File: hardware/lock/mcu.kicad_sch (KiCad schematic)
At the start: 7 parts, among them J2 DIGITAL IF (auth), J4 UPDI PROG, U1 ATtiny1616

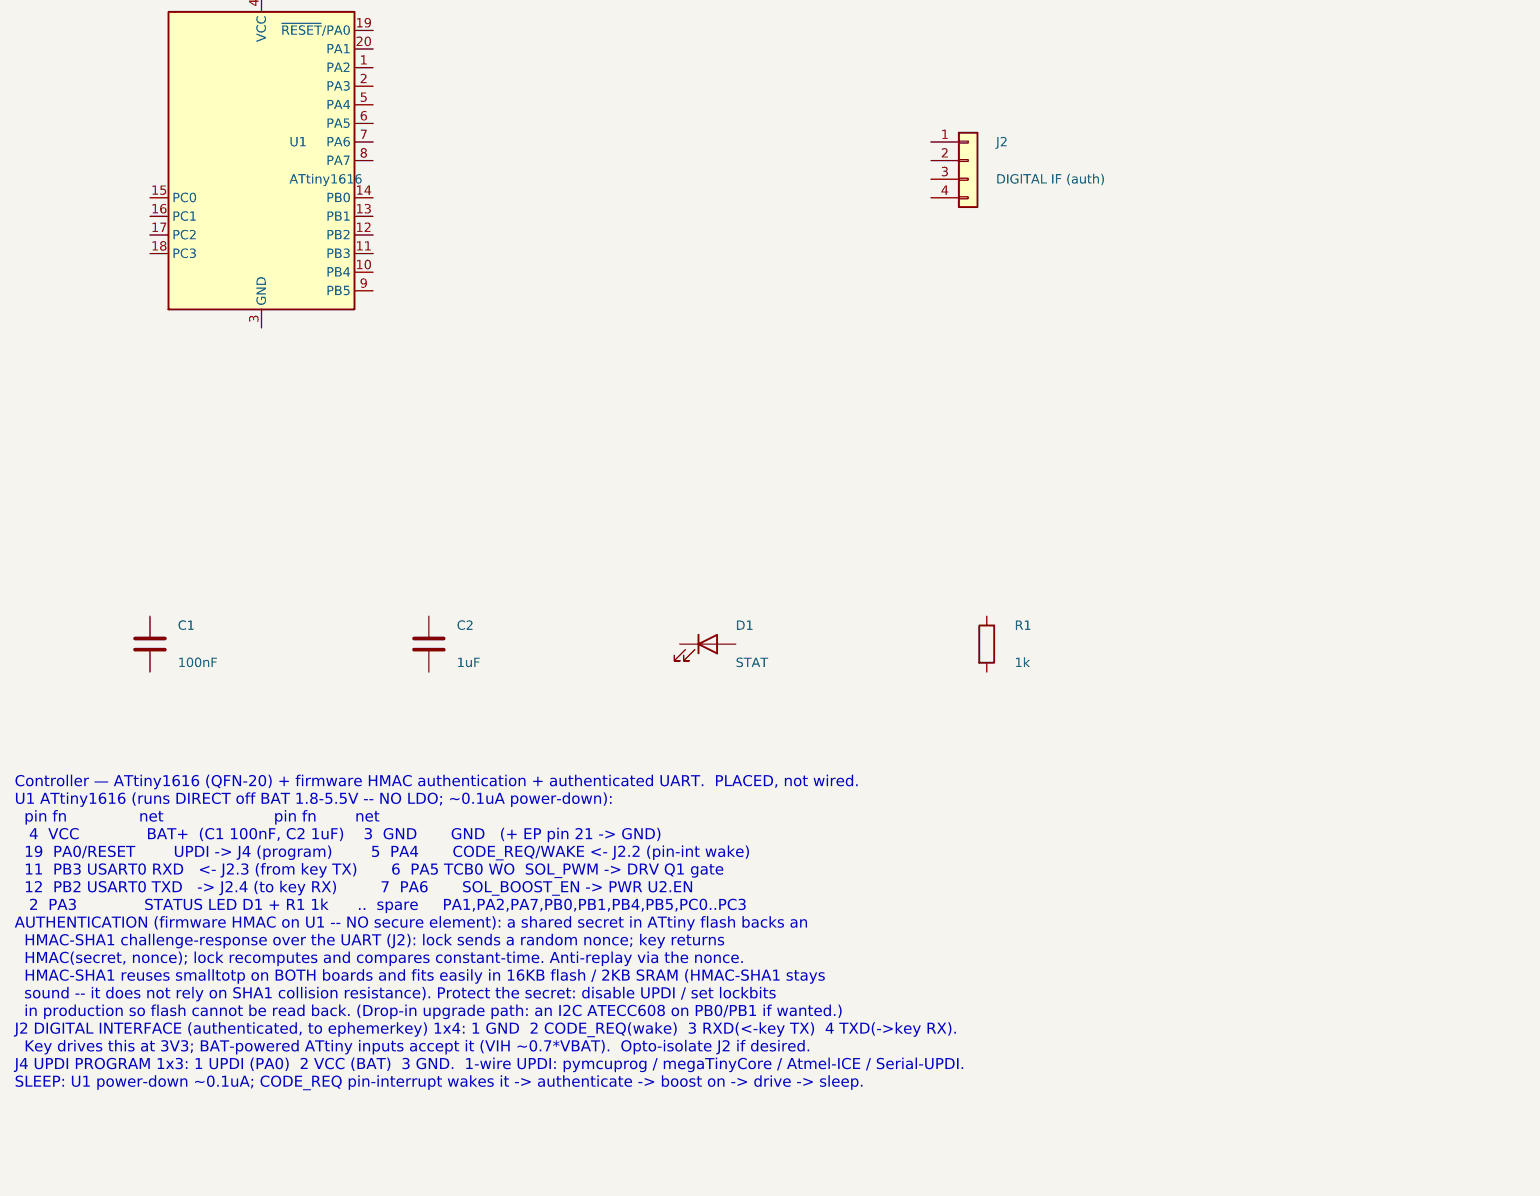
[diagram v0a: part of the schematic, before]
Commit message: lock: switch ephemerkey<->lock link to master-driven I2C (wake-on-I2C)
Replace the 4-wire authenticated UART with a 3-wire authenticated I2C bus:
- ephemerkey is the I2C master, the lock (ATtiny1616) is the target (0x60).
  Challenge-response is master-driven: read the nonce, then write the
  HMAC-SHA1(secret, nonce||code).
- Drop the discrete CODE_REQ wake line (don't mix a button-style input with
  the bus). The lock wakes from power-down on the first I2C START (pin-change
  interrupt on SCL); the master sends a dummy/wake xfer then retries.
- 3-wire J2 (GND/SCL/SDA), 1x3 on both boards.
- I2C pull-ups R11/R12 (4.7k) on ephemerkey's 3V3 (master side) -- the lock
  runs at VBAT, so master-side pull-ups avoid the 3V3/VBAT cross-domain.

ephemerkey: PB0=SDA, PB1=SCL, PB3 freed to spare; add R11/R12; regenerate.
lock: PB0=SCL+wake, PB1=SDA, PA4 freed; J2 -> 1x3; regenerate.
Docs (DESIGN.md, hardware/lock/README.md) updated to match.

Co-Authored-By: Claude Opus 4.8 (1M context) <noreply@anthropic.com>
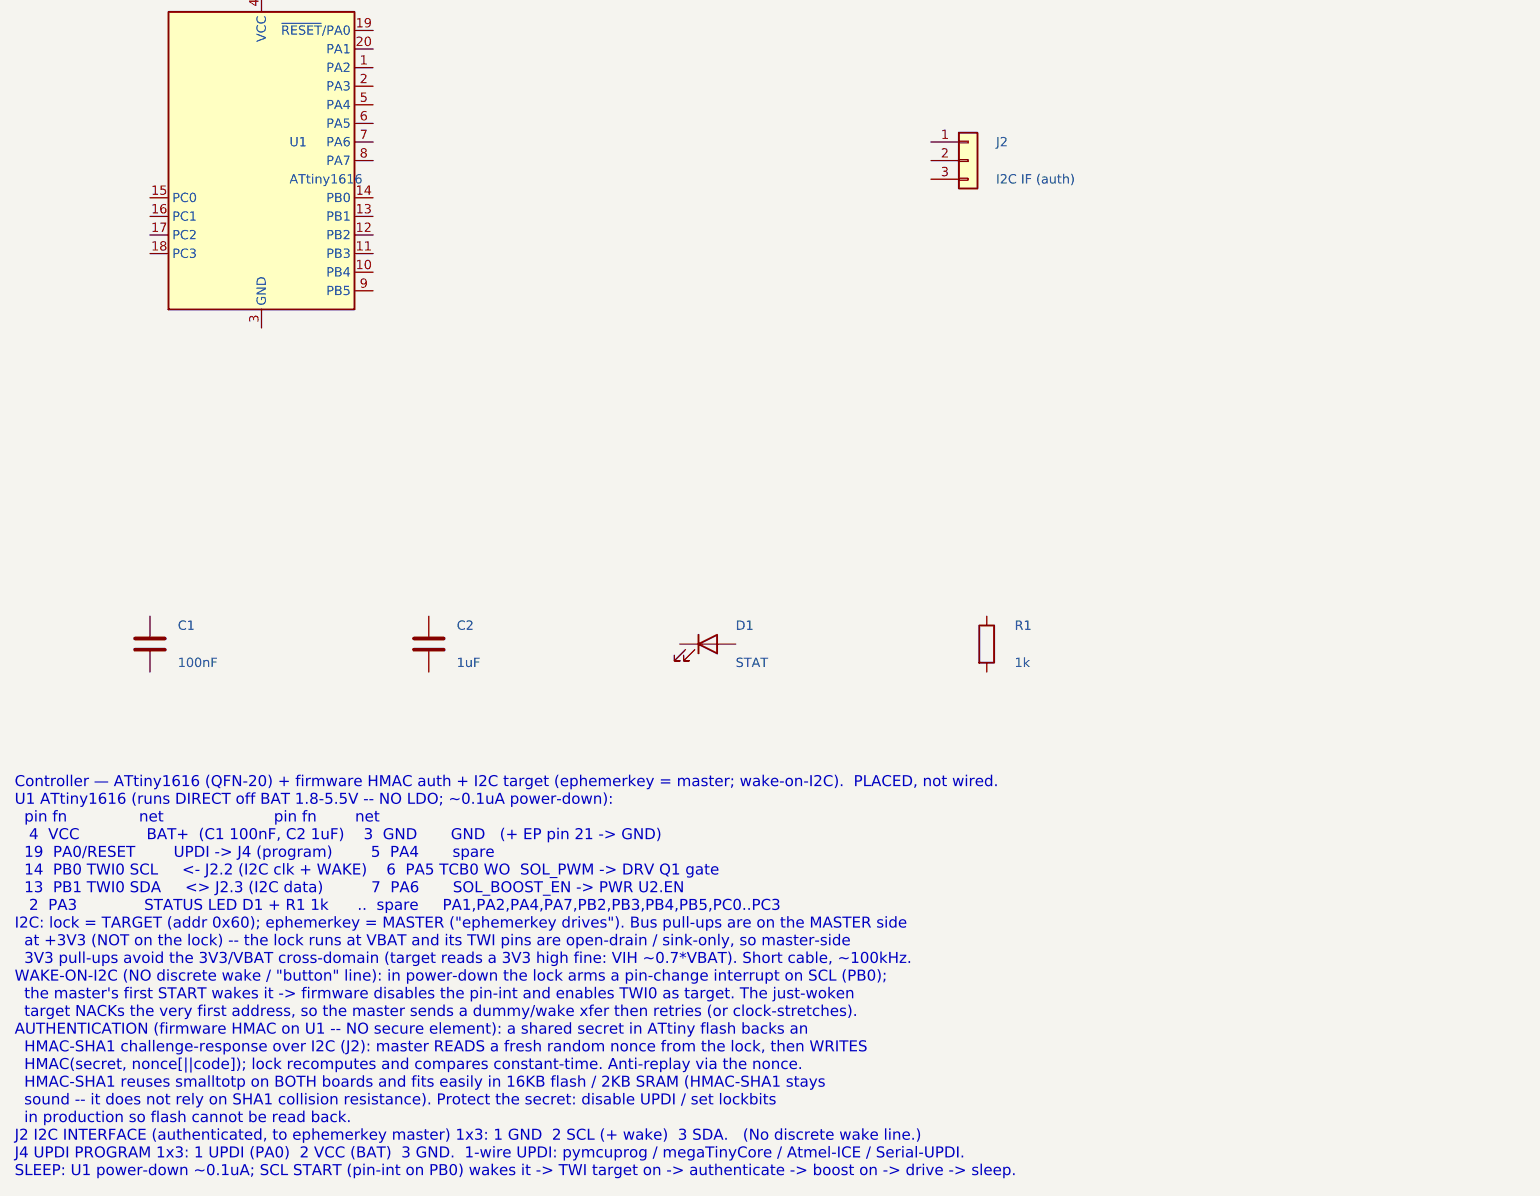
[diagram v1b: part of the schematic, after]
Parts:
- removed J2: DIGITAL IF (auth), Connector_PinHeader_2.54mm:PinHeader_1x04_P2.54mm_Vertical, symbol Connector_Generic:Conn_01x04
- added J2: I2C IF (auth), Connector_PinHeader_2.54mm:PinHeader_1x03_P2.54mm_Vertical, symbol Connector_Generic:Conn_01x03
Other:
- note added: "Controller — ATtiny1616 (QFN-20) + firmware HMAC auth + I2C target (ephemerkey = master; wake-on-I2C). PLACED, not wired. U1 ATtiny1616 (runs DIRECT off BAT 1.8-5.5V -- NO LDO; ~0.1uA power-down): pin fn net pin fn net 4 VCC BAT+ (C1 100nF, C2 1uF) 3 GND GND (+ EP pin 21 -> GND) 19 PA0/RESET UPDI -> J4 (program) 5 PA4 spare 14 PB0 TWI0 SCL <- J2.2 (I2C clk + WAKE) 6 PA5 TCB0 WO SOL_PWM -> DRV Q1 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"
- note removed: "Controller — ATtiny1616 (QFN-20) + firmware HMAC authentication + authenticated UART. PLACED, not wired. U1 ATtiny1616 (runs DIRECT off BAT 1.8-5.5V -- NO LDO; ~0.1uA power-down): pin fn net pin fn net 4 VCC BAT+ (C1 100nF, C2 1uF) 3 GND GND (+ EP pin 21 -> GND) 19 PA0/RESET UPDI -> J4 (program) 5 PA4 CODE_REQ/WAKE <- J2.2 (pin-int wake) 11 PB3 USART0 RXD <- J2.3 (from key TX) 6 PA5 TCB0 WO SOL_P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"
- title: lock — Controller (ATtiny1616) / firmware-HMAC auth / authenticated UART -> lock — Controller (ATtiny1616) / firmware-HMAC auth / authenticated I2C (target)
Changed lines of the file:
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@@
 	(paper "A3")
 	(title_block
-		(title "lock — Controller (ATtiny1616) / firmware-HMAC auth / authenticated UART")
+		(title "lock — Controller (ATtiny1616) / firmware-HMAC auth / authenticated I2C (target)")
 		(date "2026-06-28")
 		(rev "0.1")
@@
 		(instances
 			(project "lock"
-				(path "/e1000000-0000-4000-8000-000000000002/34f422b3-1977-4e3e-804d-e2379fb9eb47"
+				(path "/e1000000-0000-4000-8000-000000000002/5e503e8f-d827-48b6-ba4b-345d3c9420b5"
 					(reference "U1")
 					(unit 1)
@@
 	)
 	(symbol
-		(lib_id "Connector_Generic:Conn_01x04")
+		(lib_id "Connector_Generic:Conn_01x03")
 		(at 142.2400 55.8800 0)
 		(unit 1)
@@
 			(effects (font (size 1.27 1.27)) (justify left))
 		)
-		(property "Value" "DIGITAL IF (auth)"
+		(property "Value" "I2C IF (auth)"
 			(at 146.0500 58.4200 0)
 			(effects (font (size 1.27 1.27)) (justify left))
 		)
-		(property "Footprint" "Connector_PinHeader_2.54mm:PinHeader_1x04_P2.54mm_Vertical"
+		(property "Footprint" "Connector_PinHeader_2.54mm:PinHeader_1x03_P2.54mm_Vertical"
 			(at 142.2400 55.8800 0)
 			(effects (font (size 1.27 1.27))) (hide yes)
@@
 		(pin "2")
 		(pin "3")
-		(pin "4")
-		(instances
-			(project "lock"
-				(path "/e1000000-0000-4000-8000-000000000002/34f422b3-1977-4e3e-804d-e2379fb9eb47"
+		(instances
+			(project "lock"
+				(path "/e1000000-0000-4000-8000-000000000002/5e503e8f-d827-48b6-ba4b-345d3c9420b5"
 					(reference "J2")
 					(unit 1)
@@
 		(instances
 			(project "lock"
-				(path "/e1000000-0000-4000-8000-000000000002/34f422b3-1977-4e3e-804d-e2379fb9eb47"
+				(path "/e1000000-0000-4000-8000-000000000002/5e503e8f-d827-48b6-ba4b-345d3c9420b5"
 					(reference "J4")
 					(unit 1)
@@
 		(instances
 			(project "lock"
-				(path "/e1000000-0000-4000-8000-000000000002/34f422b3-1977-4e3e-804d-e2379fb9eb47"
+				(path "/e1000000-0000-4000-8000-000000000002/5e503e8f-d827-48b6-ba4b-345d3c9420b5"
 					(reference "C1")
 					(unit 1)
@@
 		(instances
 			(project "lock"
-				(path "/e1000000-0000-4000-8000-000000000002/34f422b3-1977-4e3e-804d-e2379fb9eb47"
+				(path "/e1000000-0000-4000-8000-000000000002/5e503e8f-d827-48b6-ba4b-345d3c9420b5"
 					(reference "C2")
 					(unit 1)
@@
 		(instances
 			(project "lock"
-				(path "/e1000000-0000-4000-8000-000000000002/34f422b3-1977-4e3e-804d-e2379fb9eb47"
+				(path "/e1000000-0000-4000-8000-000000000002/5e503e8f-d827-48b6-ba4b-345d3c9420b5"
 					(reference "D1")
 					(unit 1)
@@
 		(instances
 			(project "lock"
-				(path "/e1000000-0000-4000-8000-000000000002/34f422b3-1977-4e3e-804d-e2379fb9eb47"
+				(path "/e1000000-0000-4000-8000-000000000002/5e503e8f-d827-48b6-ba4b-345d3c9420b5"
 					(reference "R1")
 					(unit 1)
@@
 		)
 	)
-	(text "Controller — ATtiny1616 (QFN-20) + firmware HMAC authentication + authenticated UART.  PLACED, not wired.\nU1 ATtiny1616 (runs DIRECT off BAT 1.8-5.5V -- NO LDO; ~0.1uA power-down):\n  pin fn               net                       pin fn        net\n   4  VCC              BAT+  (C1 100nF, C2 1uF)    3  GND       GND   (+ EP pin 21 -> GND)\n  19  PA0/RESET        UPDI -> J4 (program)        5  PA4       CODE_REQ/WAKE <- J2.2 (pin-int wake)\n  11  PB3 USART0 RXD   <- J2.3 (from key TX)       6  PA5 TCB0 WO  SOL_PWM -> DRV Q1 gate\n  12  PB2 USART0 TXD   -> J2.4 (to key RX)         7  PA6       SOL_BOOST_EN -> PWR U2.EN\n   2  PA3              STATUS LED D1 + R1 1k      ..  spare     PA1,PA2,PA7,PB0,PB1,PB4,PB5,PC0..PC3\nAUTHENTICATION (firmware HMAC on U1 -- NO secure element): a shared secret in ATtiny flash backs an\n  HMAC-SHA1 challenge-response over the UART (J2): lock sends a random nonce; key returns\n  HMAC(secret, nonce); lock recomputes and compares constant-time. Anti-replay via the nonce.\n  HMAC-SHA1 reuses smalltotp on BOTH boards and fits easily in 16KB flash / 2KB SRAM (HMAC-SHA1 stays\n  sound -- it does not rely on SHA1 collision resistance). Protect the secret: disable UPDI / set lockbits\n  in production so flash cannot be read back. (Drop-in upgrade path: an I2C ATECC608 on PB0/PB1 if wanted.)\nJ2 DIGITAL INTERFACE (authenticated, to ephemerkey) 1x4: 1 GND  2 CODE_REQ(wake)  3 RXD(<-key TX)  4 TXD(->key RX).\n  Key drives this at 3V3; BAT-powered ATtiny inputs accept it (VIH ~0.7*VBAT).  Opto-isolate J2 if desired.\nJ4 UPDI PROGRAM 1x3: 1 UPDI (PA0)  2 VCC (BAT)  3 GND.  1-wire UPDI: pymcuprog / megaTinyCore / Atmel-ICE / Serial-UPDI.\nSLEEP: U1 power-down ~0.1uA; CODE_REQ pin-interrupt wakes it -> authenticate -> boost on -> drive -> sleep."
+	(text "Controller — ATtiny1616 (QFN-20) + firmware HMAC auth + I2C target (ephemerkey = master; wake-on-I2C).  PLACED, not wired.\nU1 ATtiny1616 (runs DIRECT off BAT 1.8-5.5V -- NO LDO; ~0.1uA power-down):\n  pin fn               net                       pin fn        net\n   4  VCC              BAT+  (C1 100nF, C2 1uF)    3  GND       GND   (+ EP pin 21 -> GND)\n  19  PA0/RESET        UPDI -> J4 (program)        5  PA4       spare\n  14  PB0 TWI0 SCL     <- J2.2 (I2C clk + WAKE)    6  PA5 TCB0 WO  SOL_PWM -> DRV Q1 gate\n  13  PB1 TWI0 SDA     <> J2.3 (I2C data)          7  PA6       SOL_BOOST_EN -> PWR U2.EN\n   2  PA3              STATUS LED D1 + R1 1k      ..  spare     PA1,PA2,PA4,PA7,PB2,PB3,PB4,PB5,PC0..PC3\nI2C: lock = TARGET (addr 0x60); ephemerkey = MASTER (\"ephemerkey drives\"). Bus pull-ups are on the MASTER side\n  at +3V3 (NOT on the lock) -- the lock runs at VBAT and its TWI pins are open-drain / sink-only, so master-side\n  3V3 pull-ups avoid the 3V3/VBAT cross-domain (target reads a 3V3 high fine: VIH ~0.7*VBAT). Short cable, ~100kHz.\nWAKE-ON-I2C (NO discrete wake / \"button\" line): in power-down the lock arms a pin-change interrupt on SCL (PB0);\n  the master's first START wakes it -> firmware disables the pin-int and enables TWI0 as target. The just-woken\n  target NACKs the very first address, so the master sends a dummy/wake xfer then retries (or clock-stretches).\nAUTHENTICATION (firmware HMAC on U1 -- NO secure element): a shared secret in ATtiny flash backs an\n  HMAC-SHA1 challenge-response over I2C (J2): master READS a fresh random nonce from the lock, then WRITES\n  HMAC(secret, nonce[||code]); lock recomputes and compares constant-time. Anti-replay via the nonce.\n  HMAC-SHA1 reuses smalltotp on BOTH boards and fits easily in 16KB flash / 2KB SRAM (HMAC-SHA1 stays\n  sound -- it does not rely on SHA1 collision resistance). Protect the secret: disable UPDI / set lockbits\n  in production so flash cannot be read back.\nJ2 I2C INTERFACE (authenticated, to ephemerkey master) 1x3: 1 GND  2 SCL (+ wake)  3 SDA.   (No discrete wake line.)\nJ4 UPDI PROGRAM 1x3: 1 UPDI (PA0)  2 VCC (BAT)  3 GND.  1-wire UPDI: pymcuprog / megaTinyCore / Atmel-ICE / Serial-UPDI.\nSLEEP: U1 power-down ~0.1uA; SCL START (pin-int on PB0) wakes it -> TWI target on -> authenticate -> boost on -> drive -> sleep."
 		(exclude_from_sim no)
 		(at 12.00 140.00 0)

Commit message: lock: servo option, firmware boost/power control, hall sensors, I2C protocol
Checkpoint of the companion lock board evolution:
- I2C link connector -> right-angle 4-pin JST-PH (S4B-PH-K, C157926);
  VCC is No-Connect on the lock (don't bridge the two battery rails).
- Add a parallel servo actuator option (J5) beside the 12V solenoid; one
  fully-populated board can carry both, one active at a time.
- Firmware-selectable boost: BOOST_VSEL (Q2 + R17 switch the FB divider)
  -> 6V (servo, default) or 12V (solenoid).  R4 22k / R17 20k.
- Servo high-side load switch (Q3 P-FET + Q4 driver, SERVO_PWR_EN) with a
  hardware interlock (Q5) that forces servo power OFF whenever boost = 12V,
  so a 12V solenoid pulse can never reach a 6V servo.
- Door/bolt hall sensors (J6/J7, S3B-PH-K) powered from a GPIO (HALL_PWR)
  so they draw ~0uA when the lock sleeps.
- I2C register/command protocol: STATUS (door/bolt/actuator probe, no auth),
  NONCE (read), COMMAND (authenticated UNLOCK/LOCK; LOCK drives a servo to the
  lock angle).  HMAC-SHA1 challenge-response, reuses smalltotp.

All footprints are KiCad-bundled (every part carries a 3D model). Board
regenerates + checks clean (46 components). Docs: hardware/lock/README.md and
DESIGN.md updated.

Co-Authored-By: Claude Opus 4.8 (1M context) <noreply@anthropic.com>
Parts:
- removed J2: I2C IF (auth), Connector_PinHeader_2.54mm:PinHeader_1x03_P2.54mm_Vertical, symbol Connector_Generic:Conn_01x03
- added C10, C9: 100nF, Capacitor_SMD:C_0402_1005Metric, symbol Device:C
- added J2: I2C JST-PH RA, Connector_JST:JST_PH_S4B-PH-K_1x04_P2.00mm_Horizontal, symbol Connector_Generic:Conn_01x04
- added J6: HALL DOOR, Connector_JST:JST_PH_S3B-PH-K_1x03_P2.00mm_Horizontal, symbol Connector_Generic:Conn_01x03
- added J7: HALL BOLT, Connector_JST:JST_PH_S3B-PH-K_1x03_P2.00mm_Horizontal, symbol Connector_Generic:Conn_01x03
- added R22, R23: 10k, Resistor_SMD:R_0402_1005Metric, symbol Device:R
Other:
- note added: "Controller — ATtiny1616 (QFN-20) + firmware HMAC auth + I2C target (ephemerkey = master; wake-on-I2C). PLACED, not wired. U1 ATtiny1616 (runs DIRECT off BAT 1.8-5.5V -- NO LDO; ~0.1uA power-down): pin fn net pin fn net 4 VCC BAT+ (C1 100nF, C2 1uF) 3 GND GND (+ EP pin 21 -> GND) 19 PA0/RESET UPDI -> J4 (program) 5 PA4 HALL_PWR -> J6/J7 V+ (gated low-power) 14 PB0 TWI0 SCL <- J2.4 (I2C clk + WAKE)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"
- note removed: "Controller — ATtiny1616 (QFN-20) + firmware HMAC auth + I2C target (ephemerkey = master; wake-on-I2C). PLACED, not wired. U1 ATtiny1616 (runs DIRECT off BAT 1.8-5.5V -- NO LDO; ~0.1uA power-down): pin fn net pin fn net 4 VCC BAT+ (C1 100nF, C2 1uF) 3 GND GND (+ EP pin 21 -> GND) 19 PA0/RESET UPDI -> J4 (program) 5 PA4 spare 14 PB0 TWI0 SCL <- J2.2 (I2C clk + WAKE) 6 PA5 TCB0 WO SOL_PWM -> DRV Q1 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"

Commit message: lock: second servo output, clearer wiring notes, start PCB layout
- Add a second servo output (J8 + SERVO_SIG2 on PB4, R24/R25) sharing the
  VSERVO rail and the load-switch/interlock -- e.g. a dual-latch lock.
- Rewrite the per-sheet wiring notes (MCU/PWR/DRV) from prose into terse
  pin -> net maps: one line per part, every pin = its net, with a NETS IN
  header for cross-sheet signals. Rationale stays in the README.
- kschgen: park the wiring note below all placed components so the text no
  longer overlaps symbols (computed from the last component row).
- Start the lock PCB layout (hardware/lock/lock.kicad_pcb).

Board regenerates + checks clean (49 components; all footprints carry 3D models).

Co-Authored-By: Claude Opus 4.8 (1M context) <noreply@anthropic.com>
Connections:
- net HAL_PWR: now reaches J6.1 (Pin_1)
- net HAL_PWR: now also J7.1 (Pin_1), R22.1, R23.1, U1.5 (PA4)
- net GND: now reaches J6.2 (Pin_2)
- net GND: now also C1.2, C10.2, C2.2, C9.2, J2.1 (Pin_1), J4.3 (Pin_3), J7.2 (Pin_2), R1.2, U1.21 (GND), U1.3 (GND)
- net HALL_DOOR: now reaches J6.3 (Pin_3)
- net HALL_DOOR: now also C10.1, R23.2, U1.8 (PA7)
- net SERVO_PWR_EN: now reaches U1.1 (PA2)
- net SERVO_SIG2: now reaches U1.10 (PB4)
- net HALL_BOLT: now reaches U1.11 (PB3)
- net HALL_BOLT: now also C9.1, J7.3 (Pin_3), R22.2
- net SERVO_SIG: now reaches U1.12 (PB2)
- net SDA: now reaches U1.13 (PB1)
- net SDA: now also J2.3 (Pin_3)
- net SCL: now reaches U1.14 (PB0)
- net SCL: now also J2.4 (Pin_4)
- net at U1.18 (PC3): now also D1.2 (A)
- net at U1.19 (~{RESET}/PA0): now also J4.1 (Pin_1)
- net BOOST_VSEL: now reaches U1.20 (PA1)
- net VCC: now reaches U1.4 (VCC)
- net VCC: now also C1.1, C2.1, J2.2 (Pin_2), J4.2 (Pin_2)
- net SOL_PWM: now reaches U1.6 (PA5)
- net SOL_BOOST_EN: now reaches U1.7 (PA6)
- net at R1.1: now also D1.1 (K)
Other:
- note added: "MCU — ATtiny1616 (QFN-20) controller. Pinout / nets (PLACED, not wired). Runs off BAT, no LDO. pin name net pin name net 4 VCC BAT+ (C1, C2 to GND) 3 GND GND (+ EP pin 21) 19 PA0/RESET UPDI = J4.1 5 PA4 HALL_PWR -> J6.1, J7.1, R22, R23 14 PB0 SCL = J2.4 (I2C clk + wake) 6 PA5 SOL_PWM -> DRV R5 13 PB1 SDA = J2.3 (I2C data) 7 PA6 SOL_BOOST_EN -> PWR U2.EN 2 PA3 LED: PA3 -> D1 -> R1 -> GND 8 PB2 SER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"
- note removed: "Controller — ATtiny1616 (QFN-20) + firmware HMAC auth + I2C target (ephemerkey = master; wake-on-I2C). PLACED, not wired. U1 ATtiny1616 (runs DIRECT off BAT 1.8-5.5V -- NO LDO; ~0.1uA power-down): pin fn net pin fn net 4 VCC BAT+ (C1 100nF, C2 1uF) 3 GND GND (+ EP pin 21 -> GND) 19 PA0/RESET UPDI -> J4 (program) 5 PA4 HALL_PWR -> J6/J7 V+ (gated low-power) 14 PB0 TWI0 SCL <- J2.4 (I2C clk + WAKE)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"
